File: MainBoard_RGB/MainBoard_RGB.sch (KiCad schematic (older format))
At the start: 14 parts, among them J1 Conn_01x02_Female, J2 Conn_02x03_Top_Bottom, J3 Conn_01x04_Female, Q1 Q_NMOS_DGS, Q2 Q_NMOS_DGS, Q3 Q_NMOS_DGS, U1 ESP-01v090, U2 AZ1117-3.3, U3 ATTINY85-20PU

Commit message: RGB platform finished
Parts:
- added C3: 10uF, Capacitors_SMD:C_0805_HandSoldering, symbol C
- added PS1: VX7805-500, VX7805-500:VX7805500, symbol VX7805-500
- J2: footprint Connectors_Phoenix:PhoenixContact_MCV-G_02x5.08mm_Vertical -> Connectors_Samtec:SDL-106-X-XX_2x03
- Q1, Q2, Q3: footprint TO_SOT_Packages_SMD:SOT-23 -> TO_SOT_Packages_SMD:TO-252-2
- U3: footprint Housings_DIP:DIP-8_W7.62mm -> Housings_SOIC:SO-8_5.3x6.2mm_Pitch1.27mm
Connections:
- net +5V: now also PS1.3 (+VOUT)
- net GND: now also C3.2, PS1.2 (GND)
- net VDD: now also C3.1, PS1.1 (+VIN)
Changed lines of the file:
@@
 LIBS:contrib
 LIBS:valves
-LIBS:ESP8266
-LIBS:RAC01-05SGB
+LIBS:VX7805-500
 LIBS:MainBoard_RGB-cache
 EELAYER 25 0
@@
 L GND #PWR02
 U 1 1 5B52EDFD
-P 9300 1350
-F 0 "#PWR02" H 9300 1100 50  0001 C CNN
-F 1 "GND" H 9300 1200 50  0000 C CNN
-F 2 "" H 9300 1350 50  0001 C CNN
-F 3 "" H 9300 1350 50  0001 C CNN
-	1    9300 1350
+P 9300 1400
+F 0 "#PWR02" H 9300 1150 50  0001 C CNN
+F 1 "GND" H 9300 1250 50  0000 C CNN
+F 2 "" H 9300 1400 50  0001 C CNN
+F 3 "" H 9300 1400 50  0001 C CNN
+	1    9300 1400
 	1    0    0    -1
 $EndComp
@@
 F 0 "Q1" H 5300 1950 50  0000 L CNN
 F 1 "Q_NMOS_DGS" H 5300 1850 50  0000 L CNN
-F 2 "TO_SOT_Packages_SMD:SOT-23" H 5300 2000 50  0001 C CNN
+F 2 "TO_SOT_Packages_SMD:TO-252-2" H 5300 2000 50  0001 C CNN
 F 3 "" H 5100 1900 50  0001 C CNN
 	1    5100 1900
@@
 F 0 "Q2" H 6250 1950 50  0000 L CNN
 F 1 "Q_NMOS_DGS" H 6250 1850 50  0000 L CNN
-F 2 "TO_SOT_Packages_SMD:SOT-23" H 6250 2000 50  0001 C CNN
+F 2 "TO_SOT_Packages_SMD:TO-252-2" H 6250 2000 50  0001 C CNN
 F 3 "" H 6050 1900 50  0001 C CNN
 	1    6050 1900
@@
 F 0 "Q3" H 7100 1950 50  0000 L CNN
 F 1 "Q_NMOS_DGS" H 7100 1850 50  0000 L CNN
-F 2 "TO_SOT_Packages_SMD:SOT-23" H 7100 2000 50  0001 C CNN
+F 2 "TO_SOT_Packages_SMD:TO-252-2" H 7100 2000 50  0001 C CNN
 F 3 "" H 6900 1900 50  0001 C CNN
 	1    6900 1900
@@
 F 0 "U3" H 4750 4800 50  0000 C CNN
 F 1 "ATTINY85-20PU" H 6900 4000 50  0000 C CNN
-F 2 "Housings_DIP:DIP-8_W7.62mm" H 6900 4400 50  0001 C CIN
+F 2 "Housings_SOIC:SO-8_5.3x6.2mm_Pitch1.27mm" H 6900 4400 50  0001 C CIN
 F 3 "" H 5900 4400 50  0001 C CNN
 	1    5900 4400
@@
 F 0 "J2" H 9500 4500 50  0000 C CNN
 F 1 "Conn_02x03_Top_Bottom" H 9500 4100 50  0000 C CNN
-F 2 "Connectors_Phoenix:PhoenixContact_MCV-G_02x5.08mm_Vertical" H 9450 4300 50  0001 C CNN
+F 2 "Connectors_Samtec:SDL-106-X-XX_2x03" H 9450 4300 50  0001 C CNN
 F 3 "" H 9450 4300 50  0001 C CNN
 	1    9450 4300
@@
 	8600 4300 8600 4200
 $Comp
-L GND #PWR013
+L GND #PWR012
 U 1 1 5B5255D7
 P 8600 4300
-F 0 "#PWR013" H 8600 4050 50  0001 C CNN
+F 0 "#PWR012" H 8600 4050 50  0001 C CNN
 F 1 "GND" H 8600 4150 50  0000 C CNN
 F 2 "" H 8600 4300 50  0001 C CNN
@@
 	8700 4400 8700 4050
 $Comp
-L +3V3 #PWR014
+L +3V3 #PWR013
 U 1 1 5B5257A8
 P 8700 4050
-F 0 "#PWR014" H 8700 3900 50  0001 C CNN
+F 0 "#PWR013" H 8700 3900 50  0001 C CNN
 F 1 "+3V3" H 8700 4190 50  0000 C CNN
 F 2 "" H 8700 4050 50  0001 C CNN
@@
 	7350 4650 7350 4750
 $Comp
-L GND #PWR015
+L GND #PWR014
 U 1 1 5B525DAA
 P 7350 4750
-F 0 "#PWR015" H 7350 4500 50  0001 C CNN
+F 0 "#PWR014" H 7350 4500 50  0001 C CNN
 F 1 "GND" H 7350 4600 50  0000 C CNN
 F 2 "" H 7350 4750 50  0001 C CNN
@@
 $EndComp
 $Comp
-L +3V3 #PWR016
+L +3V3 #PWR015
 U 1 1 5B525DDF
 P 7350 4050
-F 0 "#PWR016" H 7350 3900 50  0001 C CNN
+F 0 "#PWR015" H 7350 3900 50  0001 C CNN
 F 1 "+3V3" H 7350 4190 50  0000 C CNN
 F 2 "" H 7350 4050 50  0001 C CNN
@@
 NoConn ~ 6900 3150
 $Comp
-L VDD #PWR017
+L VDD #PWR016
 U 1 1 5B52654E
 P 9150 2100
-F 0 "#PWR017" H 9150 1950 50  0001 C CNN
+F 0 "#PWR016" H 9150 1950 50  0001 C CNN
 F 1 "VDD" H 9150 2250 50  0000 C CNN
 F 2 "" H 9150 2100 50  0001 C CNN
@@
 B
 $Comp
-L +5V #PWR?
+L +5V #PWR017
 U 1 1 5B5279B3
-P 8300 1050
-F 0 "#PWR?" H 8300 900 50  0001 C CNN
-F 1 "+5V" H 8300 1190 50  0000 C CNN
-F 2 "" H 8300 1050 50  0001 C CNN
-F 3 "" H 8300 1050 50  0001 C CNN
-	1    8300 1050
-	1    0    0    -1
-$EndComp
+P 8300 900
+F 0 "#PWR017" H 8300 750 50  0001 C CNN
+F 1 "+5V" H 8300 1040 50  0000 C CNN
+F 2 "" H 8300 900 50  0001 C CNN
+F 3 "" H 8300 900 50  0001 C CNN
+	1    8300 900
+	1    0    0    -1
+$EndComp
+$Comp
+L VX7805-500 PS1
+U 1 1 5B524FC8
+P 2750 1600
+F 0 "PS1" H 3600 1800 50  0000 L CNN
+F 1 "VX7805-500" H 3000 1800 50  0000 L CNN
+F 2 "VX7805-500:VX7805500" H 3800 1700 50  0001 L CNN
+F 3 "https://www.cui.com/product/resource/vx78-500.pdf" H 3800 1600 50  0001 L CNN
+F 4 "Non-Isolated DC/DC Converters 6.5-36Vin 5Vout 0.5A 2.5W SIP non-Iso" H 3800 1500 50  0001 L CNN "Description"
+F 5 "10" H 3800 1400 50  0001 L CNN "Height"
+F 6 "CUI" H 3800 1300 50  0001 L CNN "Manufacturer_Name"
+F 7 "VX7805-500" H 3800 1200 50  0001 L CNN "Manufacturer_Part_Number"
+F 8 "" H 3800 1100 50  0001 L CNN "RS Part Number"
+F 9 "" H 3800 1000 50  0001 L CNN "RS Price/Stock"
+F 10 "VX7805-500" H 3800 900 50  0001 L CNN "Arrow Part Number"
+F 11 "https://www.arrow.com/en/products/vx7805-500/cui-inc" H 3800 800 50  0001 L CNN "Arrow Price/Stock"
+	1    2750 1600
+	1    0    0    -1
+$EndComp
+$Comp
+L VDD #PWR018
+U 1 1 5B5251AC
+P 2650 1500
+F 0 "#PWR018" H 2650 1350 50  0001 C CNN
+F 1 "VDD" H 2650 1650 50  0000 C CNN
+F 2 "" H 2650 1500 50  0001 C CNN
+F 3 "" H 2650 1500 50  0001 C CNN
+	1    2650 1500
+	1    0    0    -1
+$EndComp
+Wire Wire Line
+	2750 1600 2650 1600
+Wire Wire Line
+	2650 1600 2650 1500
+$Comp
+L GND #PWR019
+U 1 1 5B52528F
+P 2650 1800
+F 0 "#PWR019" H 2650 1550 50  0001 C CNN
+F 1 "GND" H 2650 1650 50  0000 C CNN
+F 2 "" H 2650 1800 50  0001 C CNN
+F 3 "" H 2650 1800 50  0001 C CNN
+	1    2650 1800
+	1    0    0    -1
+$EndComp
+Wire Wire Line
+	2650 1800 2650 1700
+Wire Wire Line
+	2650 1700 2750 1700
+Wire Wire Line
+	3950 1600 4050 1600
+Wire Wire Line
+	4050 1600 4050 1500
+$Comp
+L +5V #PWR020
+U 1 1 5B52560A
+P 4050 1500
+F 0 "#PWR020" H 4050 1350 50  0001 C CNN
+F 1 "+5V" H 4050 1640 50  0000 C CNN
+F 2 "" H 4050 1500 50  0001 C CNN
+F 3 "" H 4050 1500 50  0001 C CNN
+	1    4050 1500
+	1    0    0    -1
+$EndComp
+$Comp
+L C C3
+U 1 1 5B525FFF
+P 2050 1700
+F 0 "C3" H 2075 1800 50  0000 L CNN
+F 1 "10uF" H 2075 1600 50  0000 L CNN
+F 2 "Capacitors_SMD:C_0805_HandSoldering" H 2088 1550 50  0001 C CNN
+F 3 "" H 2050 1700 50  0001 C CNN
+	1    2050 1700
+	1    0    0    -1
+$EndComp
+$Comp
+L GND #PWR021
+U 1 1 5B526005
+P 2050 1850
+F 0 "#PWR021" H 2050 1600 50  0001 C CNN
+F 1 "GND" H 2050 1700 50  0000 C CNN
+F 2 "" H 2050 1850 50  0001 C CNN
+F 3 "" H 2050 1850 50  0001 C CNN
+	1    2050 1850
+	1    0    0    -1
+$EndComp
+$Comp
+L VDD #PWR022
+U 1 1 5B52606D
+P 2050 1550
+F 0 "#PWR022" H 2050 1400 50  0001 C CNN
+F 1 "VDD" H 2050 1700 50  0000 C CNN
+F 2 "" H 2050 1550 50  0001 C CNN
+F 3 "" H 2050 1550 50  0001 C CNN
+	1    2050 1550
+	1    0    0    -1
+$EndComp
+Wire Wire Line
+	9300 1350 9300 1400
+Wire Wire Line
+	8300 1050 8300 900
+Text Label 3950 1600 0    60   ~ 0
++5V
+Text Label 1200 1350 0    60   ~ 0
++12V
+Text Label 1250 1450 0    60   ~ 0
+GND
 $EndSCHEMATC

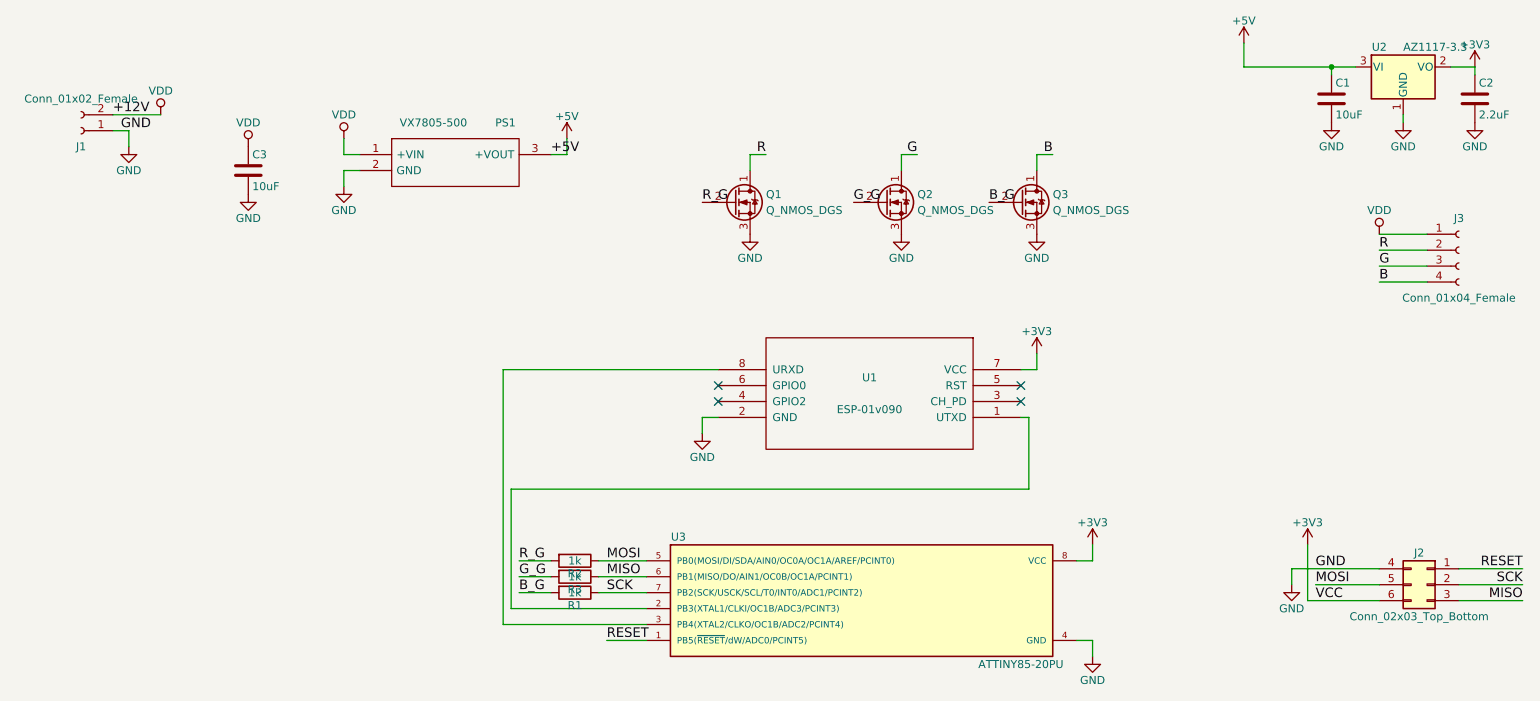
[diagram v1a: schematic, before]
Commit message: RGB and Relay platform finished
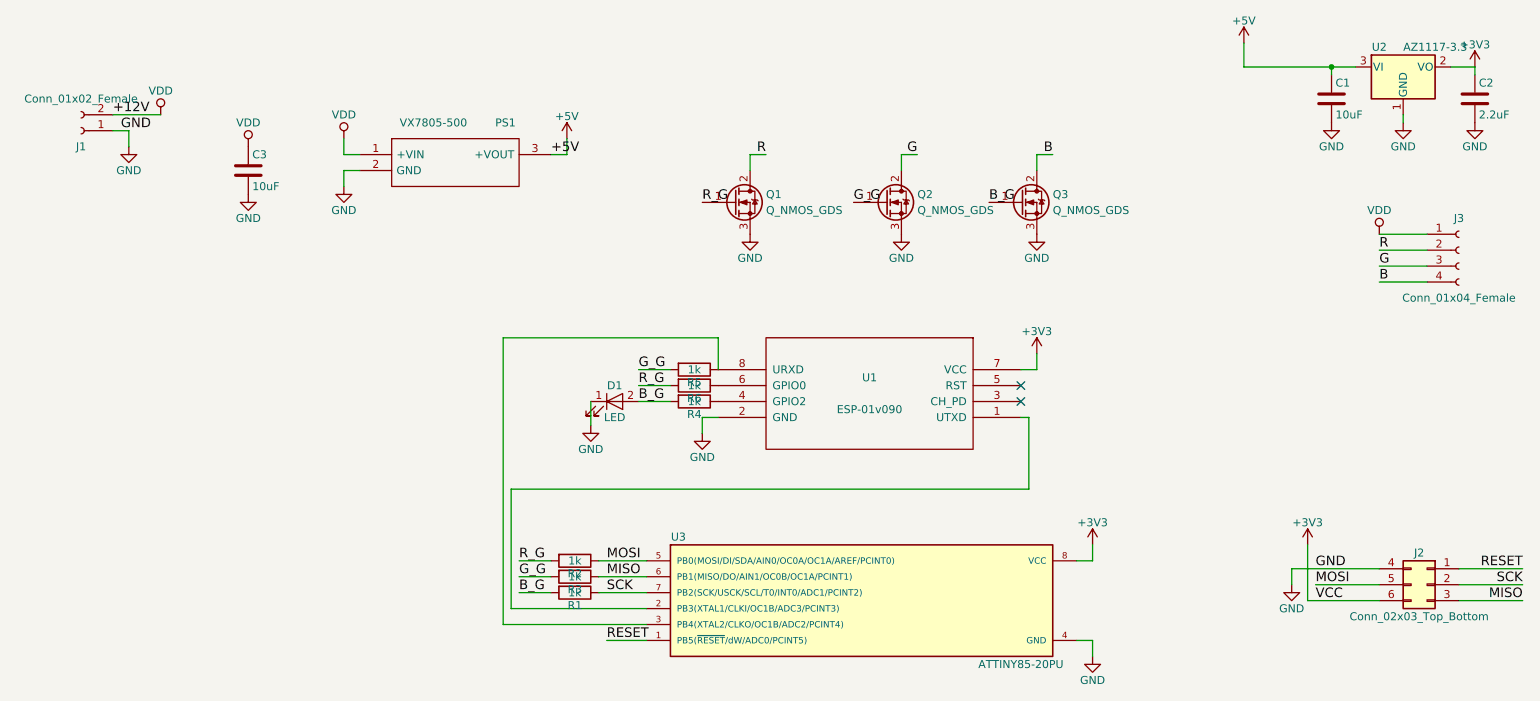
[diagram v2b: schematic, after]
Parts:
- removed Q1, Q2, Q3: Q_NMOS_DGS, TO_SOT_Packages_SMD:TO-252-2, symbol Q_NMOS_DGS
- added D1: LED, LEDs:LED_0805_HandSoldering, symbol LED
- added Q1, Q2, Q3: Q_NMOS_GDS, TO_SOT_Packages_SMD:TO-252-2, symbol Q_NMOS_GDS
- added R4, R5, R6: 1k, Resistors_SMD:R_0805_HandSoldering, symbol R
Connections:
- net B: now also Q3.2 (D)
- net B_G: now also D1.2 (A), Q3.1 (G), R4.2
- net G: now also Q2.2 (D)
- net GND: now also D1.1 (K), Q1.3 (S), Q2.3 (S), Q3.3 (S)
- net G_G: now also Q2.1 (G), R5.2
- net R: now also Q1.2 (D)
- net R_G: now also Q1.1 (G), R6.2
- net at U1.8 (URXD), U3.3 (PB4(XTAL2/CLKO/OC1B/ADC2/PCINT4)): now also R5.1
- net at U1.4 (GPIO2): now also R4.1
- net at U1.6 (GPIO0): now also R6.1
- no-connect marks 4 -> 2
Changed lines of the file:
@@
 	3950 4350 3750 4350
-$Comp
-L Q_NMOS_DGS Q1
-U 1 1 5B515147
-P 5100 1900
-F 0 "Q1" H 5300 1950 50  0000 L CNN
-F 1 "Q_NMOS_DGS" H 5300 1850 50  0000 L CNN
-F 2 "TO_SOT_Packages_SMD:TO-252-2" H 5300 2000 50  0001 C CNN
-F 3 "" H 5100 1900 50  0001 C CNN
-	1    5100 1900
-	1    0    0    -1
-$EndComp
-$Comp
-L Q_NMOS_DGS Q2
-U 1 1 5B51517E
-P 6050 1900
-F 0 "Q2" H 6250 1950 50  0000 L CNN
-F 1 "Q_NMOS_DGS" H 6250 1850 50  0000 L CNN
-F 2 "TO_SOT_Packages_SMD:TO-252-2" H 6250 2000 50  0001 C CNN
-F 3 "" H 6050 1900 50  0001 C CNN
-	1    6050 1900
-	1    0    0    -1
-$EndComp
-$Comp
-L Q_NMOS_DGS Q3
-U 1 1 5B5151B6
-P 6900 1900
-F 0 "Q3" H 7100 1950 50  0000 L CNN
-F 1 "Q_NMOS_DGS" H 7100 1850 50  0000 L CNN
-F 2 "TO_SOT_Packages_SMD:TO-252-2" H 7100 2000 50  0001 C CNN
-F 3 "" H 6900 1900 50  0001 C CNN
-	1    6900 1900
-	1    0    0    -1
-$EndComp
 $Comp
 L GND #PWR09
@@
 $EndComp
 Wire Wire Line
-	3650 2950 3650 4550
-Wire Wire Line
-	3650 2950 5000 2950
+	3650 2750 3650 4550
 Wire Wire Line
 	6900 3250 6950 3250
@@
 	1    0    0    -1
 $EndComp
-NoConn ~ 5000 3050
-NoConn ~ 5000 3150
 NoConn ~ 6900 3050
-NoConn ~ 6900 3150
 $Comp
 L VDD #PWR016
@@
 Text Label 1250 1450 0    60   ~ 0
 GND
+$Comp
+L LED D1
+U 1 1 5B5279FE
+P 4350 3150
+F 0 "D1" H 4350 3250 50  0000 C CNN
+F 1 "LED" H 4350 3050 50  0000 C CNN
+F 2 "LEDs:LED_0805_HandSoldering" H 4350 3150 50  0001 C CNN
+F 3 "" H 4350 3150 50  0001 C CNN
+	1    4350 3150
+	1    0    0    -1
+$EndComp
+$Comp
+L R R4
+U 1 1 5B527B39
+P 4850 3150
+F 0 "R4" V 4930 3150 50  0000 C CNN
+F 1 "1k" V 4850 3150 50  0000 C CNN
+F 2 "Resistors_SMD:R_0805_HandSoldering" V 4780 3150 50  0001 C CNN
+F 3 "" H 4850 3150 50  0001 C CNN
+	1    4850 3150
+	0    1    1    0
+$EndComp
+$Comp
+L GND #PWR023
+U 1 1 5B527BB9
+P 4200 3300
+F 0 "#PWR023" H 4200 3050 50  0001 C CNN
+F 1 "GND" H 4200 3150 50  0000 C CNN
+F 2 "" H 4200 3300 50  0001 C CNN
+F 3 "" H 4200 3300 50  0001 C CNN
+	1    4200 3300
+	1    0    0    -1
+$EndComp
+Wire Wire Line
+	4200 3300 4200 3150
+$Comp
+L Q_NMOS_GDS Q1
+U 1 1 5B528EF0
+P 5100 1900
+F 0 "Q1" H 5300 1950 50  0000 L CNN
+F 1 "Q_NMOS_GDS" H 5300 1850 50  0000 L CNN
+F 2 "TO_SOT_Packages_SMD:TO-252-2" H 5300 2000 50  0001 C CNN
+F 3 "" H 5100 1900 50  0001 C CNN
+	1    5100 1900
+	1    0    0    -1
+$EndComp
+$Comp
+L Q_NMOS_GDS Q2
+U 1 1 5B529023
+P 6050 1900
+F 0 "Q2" H 6250 1950 50  0000 L CNN
+F 1 "Q_NMOS_GDS" H 6250 1850 50  0000 L CNN
+F 2 "TO_SOT_Packages_SMD:TO-252-2" H 6250 2000 50  0001 C CNN
+F 3 "" H 6050 1900 50  0001 C CNN
+	1    6050 1900
+	1    0    0    -1
+$EndComp
+$Comp
+L Q_NMOS_GDS Q3
+U 1 1 5B5290C4
+P 6900 1900
+F 0 "Q3" H 7100 1950 50  0000 L CNN
+F 1 "Q_NMOS_GDS" H 7100 1850 50  0000 L CNN
+F 2 "TO_SOT_Packages_SMD:TO-252-2" H 7100 2000 50  0001 C CNN
+F 3 "" H 6900 1900 50  0001 C CNN
+	1    6900 1900
+	1    0    0    -1
+$EndComp
+Wire Wire Line
+	4500 3150 4700 3150
+Text Label 4500 3050 0    60   ~ 0
+R_G
+$Comp
+L R R6
+U 1 1 5B52A169
+P 4850 3050
+F 0 "R6" V 4930 3050 50  0000 C CNN
+F 1 "1k" V 4850 3050 50  0000 C CNN
+F 2 "Resistors_SMD:R_0805_HandSoldering" V 4780 3050 50  0001 C CNN
+F 3 "" H 4850 3050 50  0001 C CNN
+	1    4850 3050
+	0    1    1    0
+$EndComp
+Wire Wire Line
+	4500 3050 4700 3050
+$Comp
+L R R5
+U 1 1 5B52A3D2
+P 4850 2950
+F 0 "R5" V 4930 2950 50  0000 C CNN
+F 1 "1k" V 4850 2950 50  0000 C CNN
+F 2 "Resistors_SMD:R_0805_HandSoldering" V 4780 2950 50  0001 C CNN
+F 3 "" H 4850 2950 50  0001 C CNN
+	1    4850 2950
+	0    1    1    0
+$EndComp
+Wire Wire Line
+	4500 2950 4700 2950
+Text Label 4500 3150 0    60   ~ 0
+B_G
+NoConn ~ 6900 3150
+Text Label 4500 2950 0    60   ~ 0
+G_G
+Wire Wire Line
+	3650 2750 5000 2750
+Wire Wire Line
+	5000 2750 5000 2950
 $EndSCHEMATC
